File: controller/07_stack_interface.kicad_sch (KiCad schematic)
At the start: 6 parts, among them J30 TSW-115-07-S-D, J31 TSW-110-07-S-D

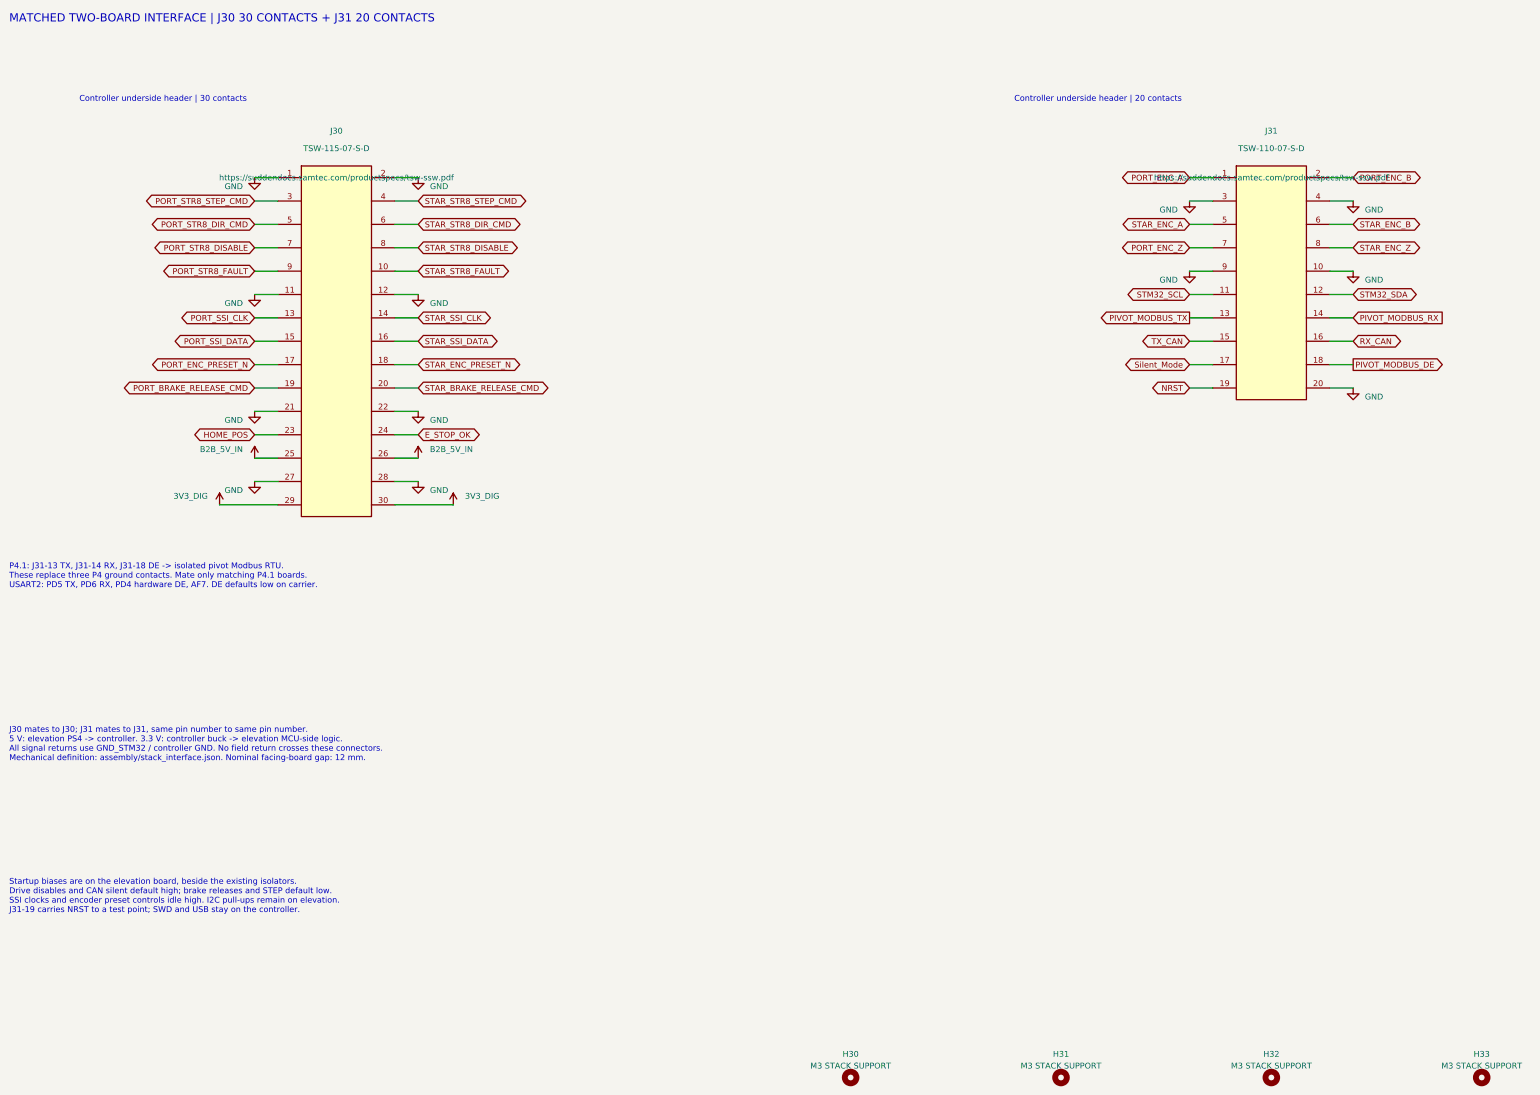
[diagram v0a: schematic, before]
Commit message: Build P6 80x130 stack with redistributed SSI and stepper interfaces
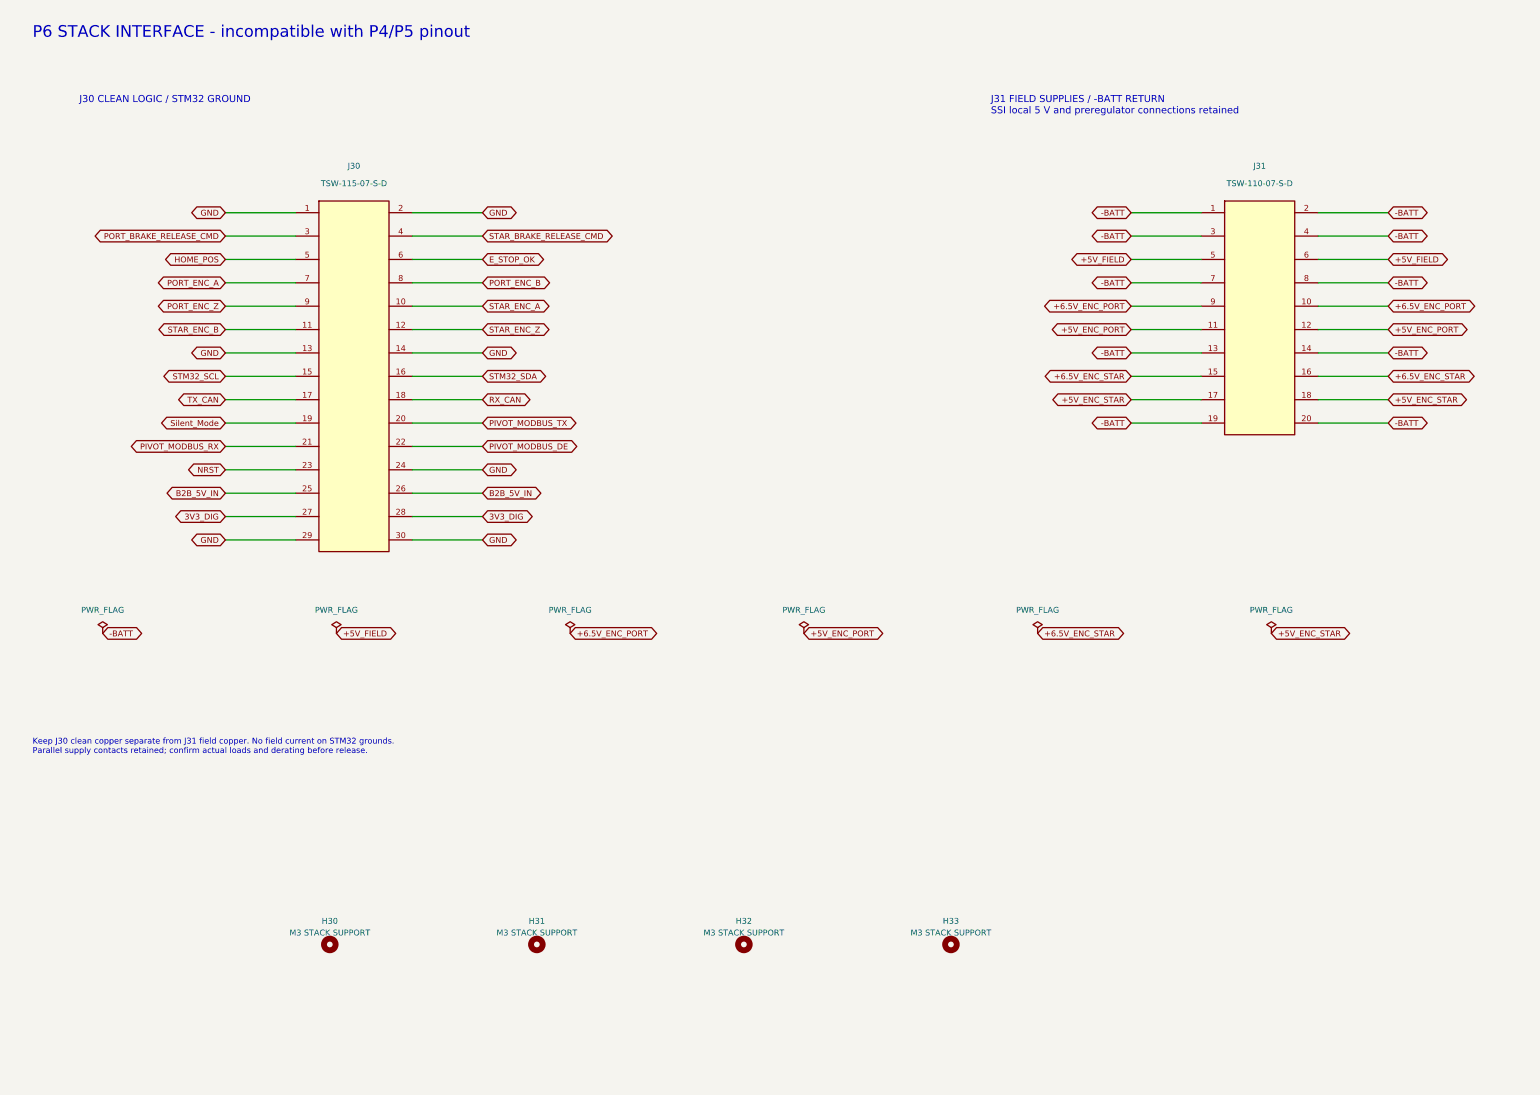
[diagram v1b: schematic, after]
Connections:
- net PORT_ENC_PRESET_N is gone; now on net TX_CAN: J30.17
- net PORT_SSI_CLK is gone; now on net GND: J30.13
- net PORT_SSI_DATA is gone; now on net STM32_SCL: J30.15
- net PORT_STR8_DIR_CMD is gone; now on net HOME_POS: J30.5
- net PORT_STR8_DISABLE is gone; now on net PORT_ENC_A: J30.7
- net PORT_STR8_FAULT is gone; now on net PORT_ENC_Z: J30.9
- net PORT_STR8_STEP_CMD is gone; now on net PORT_BRAKE_RELEASE_CMD: J30.3
- net STAR_ENC_PRESET_N is gone; now on net RX_CAN: J30.18
- net STAR_SSI_CLK is gone; now on net GND: J30.14
- net STAR_SSI_DATA is gone; now on net STM32_SDA: J30.16
- net STAR_STR8_DIR_CMD is gone; now on net E_STOP_OK: J30.6
- net STAR_STR8_DISABLE is gone; now on net PORT_ENC_B: J30.8
- net STAR_STR8_FAULT is gone; now on net STAR_ENC_A: J30.10
- net STAR_STR8_STEP_CMD is gone; now on net STAR_BRAKE_RELEASE_CMD: J30.4
- net 3V3_DIG: now also J30.27, J30.28; no longer J30.29, J30.30
- net E_STOP_OK: no longer J30.24
- net GND: now also J30.24, J30.29, J30.30; no longer J30.11, J30.12, J30.21, J30.22, J30.27, J30.28, J31.10, J31.20, J31.3, J31.4, J31.9
- net HOME_POS: no longer J30.23
- net NRST: now also J30.23; no longer J31.19
- net PIVOT_MODBUS_DE: now also J30.22; no longer J31.18
- net PIVOT_MODBUS_RX: now also J30.21; no longer J31.14
- net PIVOT_MODBUS_TX: now also J30.20; no longer J31.13
- net PORT_BRAKE_RELEASE_CMD: no longer J30.19
- net PORT_ENC_A: no longer J31.1
- net PORT_ENC_B: no longer J31.2
- net PORT_ENC_Z: no longer J31.7
- net RX_CAN: no longer J31.16
- net STAR_BRAKE_RELEASE_CMD: no longer J30.20
- net STAR_ENC_A: no longer J31.5
- net STAR_ENC_B: now also J30.11; no longer J31.6
- net STAR_ENC_Z: now also J30.12; no longer J31.8
- net STM32_SCL: no longer J31.11
- net STM32_SDA: no longer J31.12
- net Silent_Mode: now also J30.19; no longer J31.17
- net TX_CAN: no longer J31.15
- new net +5V_ENC_PORT: J31.11, J31.12
- new net +5V_ENC_STAR: J31.17, J31.18
- new net +5V_FIELD: J31.5, J31.6
- new net +6.5V_ENC_PORT: J31.10, J31.9
- new net +6.5V_ENC_STAR: J31.15, J31.16
- new net -BATT: J31.1, J31.13, J31.14, J31.19, J31.2, J31.20, J31.3, J31.4, J31.7, J31.8
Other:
- note added: "J30 CLEAN LOGIC / STM32 GROUND"
- note added: "J31 FIELD SUPPLIES / -BATT RETURN SSI local 5 V and preregulator connections retained"
- note added: "Keep J30 clean copper separate from J31 field copper. No field current on STM32 grounds. Parallel supply contacts retained; confirm actual loads and derating before release."
- note added: "P6 STACK INTERFACE - incompatible with P4/P5 pinout"
- note removed: "Controller underside header | 20 contacts"
- note removed: "Controller underside header | 30 contacts"
- note removed: "J30 mates to J30; J31 mates to J31, same pin number to same pin number. 5 V: elevation PS4 -> controller. 3.3 V: controller buck -> elevation MCU-side logic. All signal returns use GND_STM32 / controller GND. No field return crosses these connectors. Mechanical definition: assembly/stack_interface.json. Nominal facing-board gap: 12 mm."
- note removed: "MATCHED TWO-BOARD INTERFACE | J30 30 CONTACTS + J31 20 CONTACTS"
- note removed: "P4.1: J31-13 TX, J31-14 RX, J31-18 DE -> isolated pivot Modbus RTU. These replace three P4 ground contacts. Mate only matching P4.1 boards. USART2: PD5 TX, PD6 RX, PD4 hardware DE, AF7. DE defaults low on carrier."
- note removed: "Startup biases are on the elevation board, beside the existing isolators. Drive disables and CAN silent default high; brake releases and STEP default low. SSI clocks and encoder preset controls idle high. I2C pull-ups remain on elevation. J31-19 carries NRST to a test point; SWD and USB stay on the controller."
- moved on the sheet: H30, H31, H32, H33, J30, J31
